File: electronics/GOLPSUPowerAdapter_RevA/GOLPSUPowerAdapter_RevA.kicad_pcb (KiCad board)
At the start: 2 copper layers, 114.3 x 101.6 mm, 16 parts, among them P1 CONN_01X09, P10 CONN_01X09, P11 CONN_01X04, P12 CONN_01X04, P2 CONN_01X04, P3 CONN_01X04, P4 CONN_01X09, P5 CONN_01X04, P6 CONN_01X04, P7 CONN_01X09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

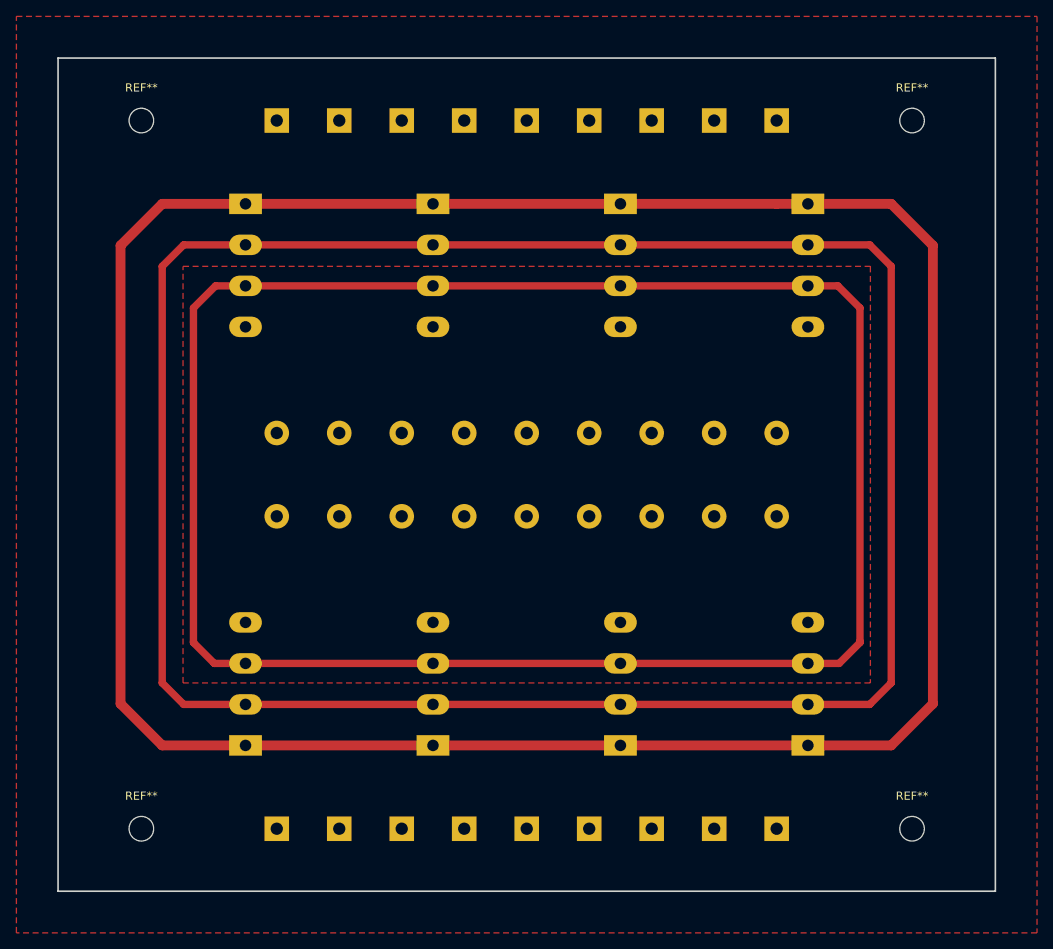
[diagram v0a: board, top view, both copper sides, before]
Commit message: modified power board to fit mill better
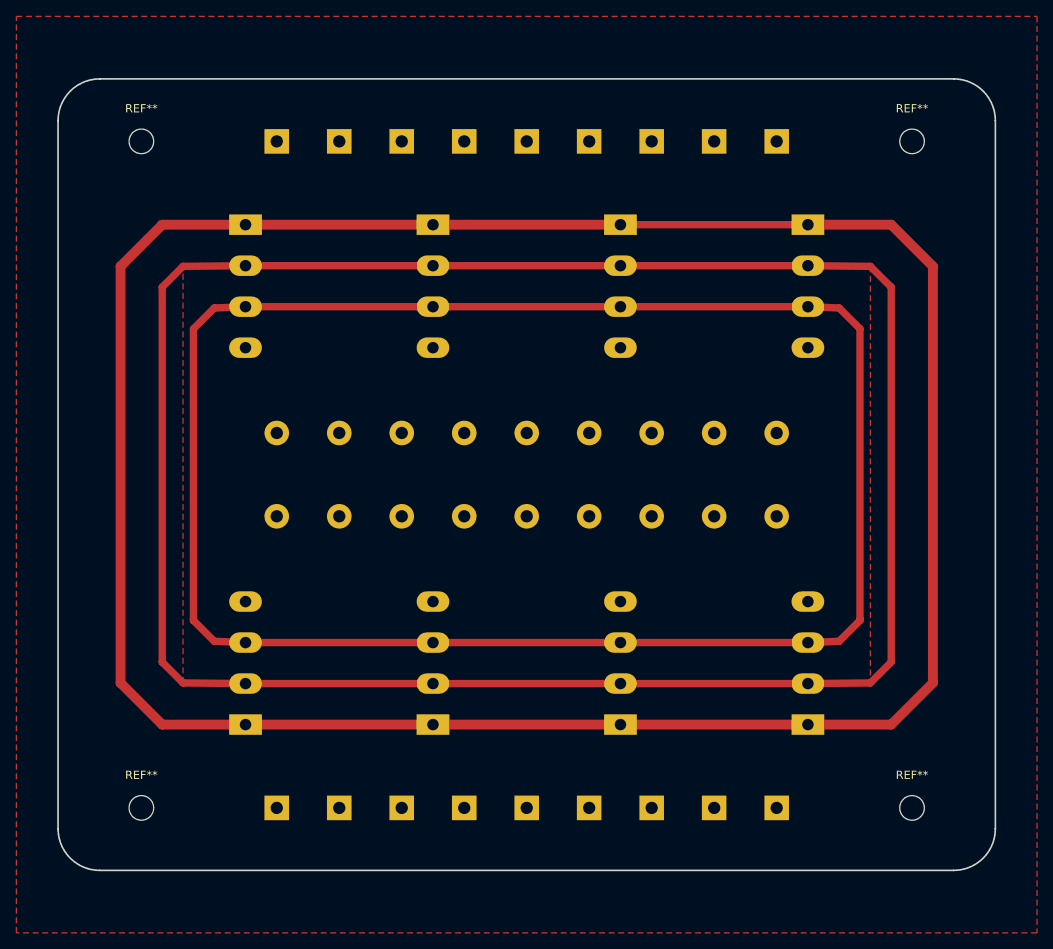
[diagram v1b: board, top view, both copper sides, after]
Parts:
- moved P1 2.54 mm to (97.8, 147.3)
- moved REF** 2.54 mm to (175.3, 147.3)
- moved REF** 2.54 mm to (81.3, 147.3)
- moved P2 2.54 mm to (94.0, 76.2)
- moved P3 2.54 mm to (116.8, 76.2)
- moved P4 2.54 mm to (97.8, 66.0)
- moved P5 2.54 mm to (139.7, 76.2)
- moved P6 2.54 mm to (162.6, 76.2)
- moved REF** 2.54 mm to (175.3, 66.0)
- moved REF** 2.54 mm to (81.3, 66.0)
- moved P11 2.54 mm to (116.8, 137.2)
- moved P12 2.54 mm to (94.0, 137.2)
- moved P8 2.54 mm to (162.6, 137.2)
- moved P9 2.54 mm to (139.7, 137.2)
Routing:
- net B: track 248.5 -> 237.9 mm
- net A: track 283.7 -> 273.5 mm
- net GND: track 318.3 -> 308.1 mm
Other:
- board size 114.3 x 101.6 mm -> 114.3 x 96.5 mm
